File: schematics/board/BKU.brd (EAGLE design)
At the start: 94 x 94 mm, 48 parts

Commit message: Исправлена БСК1
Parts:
- BSK2, BSK4: device pinheadCS:1X10 -> pinheadCS:1X11
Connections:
- net 3V3: now also BSK2.8, BSK4.8
- net GND: now also BSK2.9, BSK4.9; no longer BSK2.8, BSK4.8
- net SCL-INA: now also BSK2.10, BSK4.10; no longer BSK2.9, BSK4.9
- net SDA-INA: now also BSK2.11, BSK4.11; no longer BSK2.10, BSK4.10
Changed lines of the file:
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@@
 </autorouter>
 <elements>
-<element name="BSK2" library="pinheadCS" package="1X10" value="" x="39" y="9.9" smashed="yes">
+<element name="BSK2" library="pinheadCS" package="1X11" value="" x="39" y="9.9" smashed="yes">
 <attribute name="NAME" x="28.7638" y="6.7288" size="1.27" layer="25" ratio="10"/>
 <attribute name="VALUE" x="28.84" y="6.725" size="1.27" layer="27"/>
@@
 <attribute name="VALUE" x="87.275" y="31.76" size="1.27" layer="27" rot="R90"/>
 </element>
-<element name="BSK4" library="pinheadCS" package="1X10" value="" x="47" y="84.1" smashed="yes" rot="R180">
+<element name="BSK4" library="pinheadCS" package="1X11" value="" x="47" y="84.1" smashed="yes" rot="R180">
 <attribute name="NAME" x="64.8562" y="87.2712" size="1.27" layer="25" ratio="10" rot="R180"/>
 <attribute name="VALUE" x="64.78" y="87.275" size="1.27" layer="27" rot="R180"/>
@@
 <contactref element="BSK1" pad="9"/>
 <contactref element="BSK1" pad="11"/>
-<contactref element="BSK4" pad="8"/>
 <contactref element="BSK3" pad="9"/>
-<contactref element="BSK2" pad="8"/>
+<contactref element="BSK2" pad="9"/>
+<contactref element="BSK4" pad="9"/>
 <wire x1="82.8114" y1="76.55" x2="80.8" y2="79.1" width="0" layer="19" extent="1-1"/>
 <wire x1="85" y1="69.8" x2="84.47" y2="71.76" width="0" layer="19" extent="1-1"/>
@@
 <wire x1="32.01939375" y1="6.288" x2="30.11" y2="1.2162" width="0" layer="19" extent="1-16"/>
 <wire x1="75.7222375" y1="10.7777625" x2="70.95" y2="8.15" width="0" layer="19" extent="1-1"/>
-<wire x1="45.35" y1="9.9" x2="50.2" y2="3.3" width="0" layer="19" extent="16-16"/>
+<wire x1="46.62" y1="9.9" x2="50.2" y2="3.3" width="0" layer="19" extent="16-16"/>
 <wire x1="69.98" y1="41.3" x2="70.45" y2="33.74" width="0" layer="19" extent="1-1"/>
 <wire x1="72.52" y1="41.3" x2="69.98" y2="41.3" width="0" layer="19" extent="1-1"/>
@@
 <wire x1="56.1" y1="23.91" x2="60.48" y2="24.27" width="0" layer="19" extent="1-1"/>
 <wire x1="61.1" y1="16.77" x2="63.23" y2="23.91" width="0" layer="19" extent="1-1"/>
-<wire x1="43.55" y1="17.2" x2="45.35" y2="9.9" width="0" layer="19" extent="1-1"/>
+<wire x1="43.55" y1="17.2" x2="46.62" y2="9.9" width="0" layer="19" extent="1-1"/>
 <wire x1="39.65" y1="20.6" x2="43.55" y2="17.2" width="0" layer="19" extent="1-1"/>
 <wire x1="48.65" y1="41.25" x2="56.02" y2="36.73" width="0" layer="19" extent="1-1"/>
@@
 <wire x1="28.66" y1="36.86" x2="30.46" y2="36.97" width="0" layer="19" extent="1-1"/>
 <wire x1="29.26" y1="16" x2="30.90739375" y2="7.4" width="0" layer="19" extent="1-1"/>
-<wire x1="40.65" y1="84.1" x2="43.19" y2="93" width="0" layer="19" extent="16-16"/>
+<wire x1="39.38" y1="84.1" x2="43.19" y2="93" width="0" layer="19" extent="16-16"/>
 <wire x1="21.76" y1="25.51" x2="28.79" y2="33.47" width="0" layer="19" extent="1-1"/>
 <wire x1="11.75" y1="30.215" x2="21.76" y2="25.51" width="0" layer="19" extent="1-1"/>
@@
 <wire x1="7.1" y1="30.8" x2="9.55" y2="33.3136" width="0" layer="19" extent="1-16"/>
 <wire x1="84.1" y1="48.27" x2="72.52" y2="41.3" width="0" layer="19" extent="1-1"/>
-<wire x1="53.5" y1="77.09" x2="66.1738" y2="87.657775" width="0" layer="19" extent="1-16"/>
+<wire x1="53.5" y1="77.09" x2="39.38" y2="84.1" width="0" layer="19" extent="1-1"/>
 <wire x1="53.5" y1="61.85" x2="53.5" y2="77.09" width="0" layer="19" extent="1-1"/>
 <wire x1="8.75" y1="13.88" x2="11.75" y2="30.215" width="0" layer="19" extent="1-1"/>
@@
 <wire x1="68.6014" y1="27.5514" x2="68.125" y2="30.425" width="0" layer="19" extent="1-16"/>
 <wire x1="70.45" y1="26.12" x2="68.6014" y2="26.5514" width="0" layer="19" extent="1-16"/>
-<wire x1="42.81" y1="9.9" x2="51.875" y2="11.25" width="0" layer="19" extent="16-16"/>
-<wire x1="28.5" y1="10.875" x2="42.81" y2="9.9" width="0" layer="19" extent="16-16"/>
+<wire x1="41.54" y1="9.9" x2="51.875" y2="11.25" width="0" layer="19" extent="16-16"/>
+<wire x1="28.5" y1="10.875" x2="41.54" y2="9.9" width="0" layer="19" extent="16-16"/>
 <wire x1="53.7282" y1="82.75163125" x2="77.60483125" y2="84.875" width="0" layer="19" extent="16-16"/>
-<wire x1="43.19" y1="84.1" x2="51.25" y2="79.39516875" width="0" layer="19" extent="16-16"/>
+<wire x1="44.46" y1="84.1" x2="51.25" y2="79.39516875" width="0" layer="19" extent="16-16"/>
 <wire x1="9.9" y1="61.89" x2="7.5" y2="25.5" width="0" layer="19" extent="1-1"/>
 </signal>
@@
 <wire x1="80.8875" y1="65.2375" x2="85" y2="64.6" width="0" layer="19" extent="1-16"/>
 <wire x1="84.1" y1="38.11" x2="85.125" y2="62.625" width="0" layer="19" extent="1-1"/>
-<wire x1="48.27" y1="84.1" x2="77.043625" y2="83.625" width="0" layer="19" extent="16-16"/>
-<wire x1="28.49" y1="84.6" x2="48.27" y2="84.1" width="0" layer="19" extent="16-16"/>
+<wire x1="49.54" y1="84.1" x2="77.043625" y2="83.625" width="0" layer="19" extent="16-16"/>
+<wire x1="28.49" y1="84.6" x2="49.54" y2="84.1" width="0" layer="19" extent="16-16"/>
 <wire x1="9.9" y1="66.97" x2="13" y2="66.625" width="0" layer="19" extent="16-16"/>
 <wire x1="5.5" y1="56.125" x2="13" y2="63.75" width="0" layer="19" extent="1-1"/>
 <wire x1="12" y1="37.125" x2="7.375" y2="43.25" width="0" layer="19" extent="16-16"/>
-<wire x1="37.73" y1="9.9" x2="27.125" y2="10.375" width="0" layer="19" extent="16-16"/>
+<wire x1="36.46" y1="9.9" x2="27.125" y2="10.375" width="0" layer="19" extent="16-16"/>
 </signal>
 <signal name="N$3">
@@
 <contactref element="BSK2" pad="6"/>
 <contactref element="BSK3" pad="6"/>
-<wire x1="58.43" y1="87.43" x2="45.73" y2="84.1" width="0" layer="19" extent="16-16"/>
+<wire x1="58.43" y1="87.43" x2="47" y2="84.1" width="0" layer="19" extent="16-16"/>
 <wire x1="7.1" y1="31.6" x2="8.5" y2="31.47" width="0" layer="19" extent="1-16"/>
 <wire x1="7.1" y1="36.4" x2="7.1" y2="31.6" width="0" layer="19" extent="1-1"/>
-<wire x1="40.27" y1="9.9" x2="47.89" y2="9.601315625" width="0" layer="19" extent="16-16"/>
+<wire x1="39" y1="9.9" x2="47.89" y2="9.601315625" width="0" layer="19" extent="16-16"/>
 <wire x1="84.1" y1="40.65" x2="92.1206" y2="39.1632" width="0" layer="19" extent="16-16"/>
 <wire x1="9.9" y1="64.43" x2="8.5" y2="42.71" width="0" layer="19" extent="16-16"/>
@@
 <contactref element="BSK1" pad="8"/>
 <contactref element="BSK3" pad="8"/>
-<wire x1="9.9" y1="59.35" x2="84.1" y2="45.73" width="0" layer="19" extent="1-1"/>
+<contactref element="BSK2" pad="8"/>
+<contactref element="BSK4" pad="8"/>
+<wire x1="44.08" y1="9.9" x2="84.1" y2="45.73" width="0" layer="19" extent="1-1"/>
+<wire x1="41.92" y1="84.1" x2="84.1" y2="45.73" width="0" layer="19" extent="1-1"/>
+<wire x1="9.9" y1="59.35" x2="41.92" y2="84.1" width="0" layer="19" extent="1-1"/>
 </signal>
 <signal name="PL6-KVCC">
@@
 </signal>
 <signal name="SCL-INA">
-<contactref element="BSK2" pad="9"/>
 <contactref element="BSK3" pad="15"/>
-<contactref element="BSK4" pad="9"/>
-<wire x1="38.11" y1="84.1" x2="84.1" y2="63.51" width="0" layer="19" extent="1-1"/>
-<wire x1="47.89" y1="9.9" x2="84.1" y2="63.51" width="0" layer="19" extent="1-1"/>
+<contactref element="BSK2" pad="10"/>
+<contactref element="BSK4" pad="10"/>
+<wire x1="36.84" y1="84.1" x2="84.1" y2="63.51" width="0" layer="19" extent="1-1"/>
+<wire x1="49.16" y1="9.9" x2="84.1" y2="63.51" width="0" layer="19" extent="1-1"/>
 </signal>
 <signal name="SDA-INA">
-<contactref element="BSK2" pad="10"/>
 <contactref element="BSK3" pad="16"/>
-<contactref element="BSK4" pad="10"/>
-<wire x1="35.57" y1="84.1" x2="84.1" y2="66.05" width="0" layer="19" extent="1-1"/>
-<wire x1="50.43" y1="9.9" x2="84.1" y2="66.05" width="0" layer="19" extent="1-1"/>
+<contactref element="BSK2" pad="11"/>
+<contactref element="BSK4" pad="11"/>
+<wire x1="34.3" y1="84.1" x2="84.1" y2="66.05" width="0" layer="19" extent="1-1"/>
+<wire x1="51.7" y1="9.9" x2="84.1" y2="66.05" width="0" layer="19" extent="1-1"/>
 </signal>
 </signals>

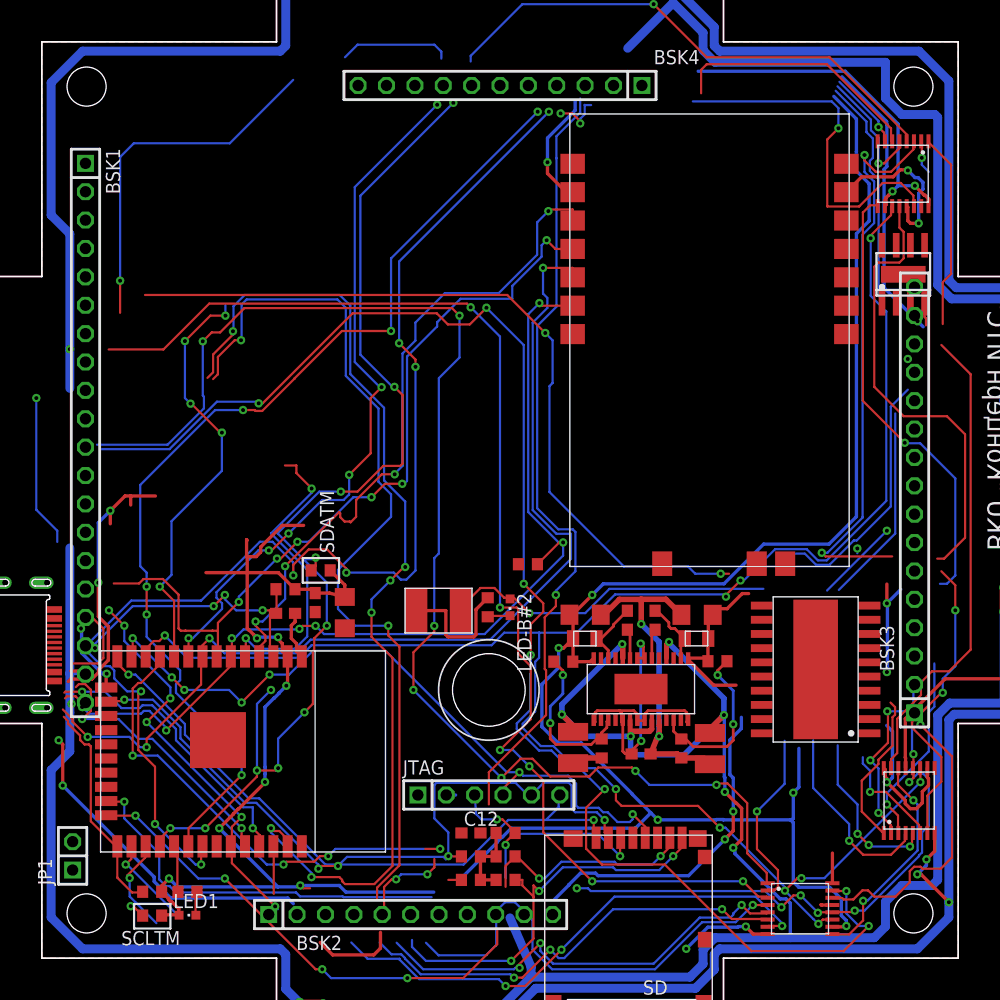
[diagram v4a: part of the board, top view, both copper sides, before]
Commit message: Обновлен список плат, работа над платой ПН
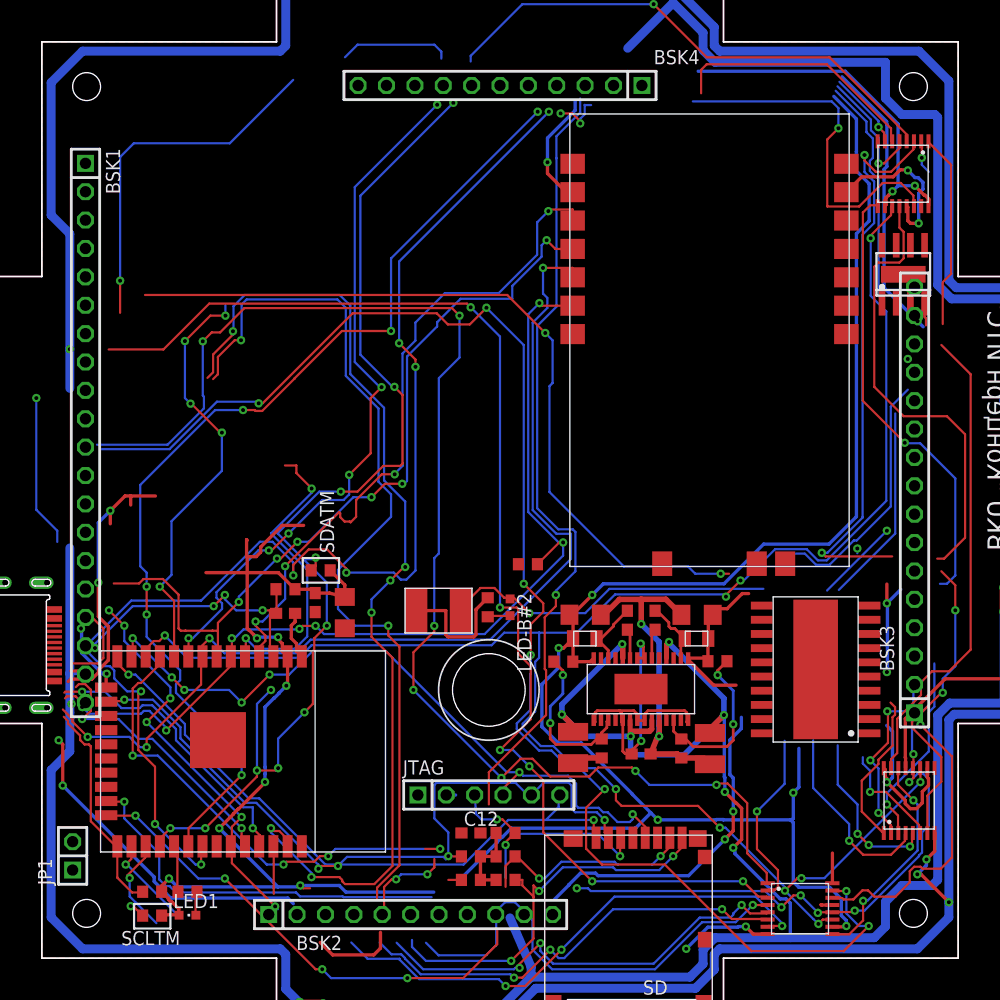
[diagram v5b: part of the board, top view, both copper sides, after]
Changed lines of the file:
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@@
 <layer number="43" name="vRestrict" color="2" fill="10" visible="no" active="yes"/>
 <layer number="44" name="Drills" color="7" fill="1" visible="no" active="yes"/>
-<layer number="45" name="Holes" color="7" fill="1" visible="no" active="yes"/>
+<layer number="45" name="Holes" color="7" fill="1" visible="yes" active="yes"/>
 <layer number="46" name="Milling" color="3" fill="1" visible="no" active="yes"/>
 <layer number="47" name="Measures" color="7" fill="1" visible="no" active="yes"/>
@@
 <wire x1="6" y1="6" x2="27" y2="6" width="0.1524" layer="20"/>
 <wire x1="27" y1="6" x2="27" y2="0" width="0.1524" layer="20"/>
-<hole x="10" y="10" drill="3.5"/>
-<hole x="84" y="84" drill="3.5"/>
-<hole x="10" y="84" drill="3.5"/>
-<hole x="84" y="10" drill="3.5"/>
+<hole x="10" y="10" drill="2.5"/>
+<hole x="84" y="84" drill="2.5"/>
+<hole x="10" y="84" drill="2.5"/>
+<hole x="84" y="10" drill="2.5"/>
 <text x="92.4" y="64.95" size="1.778" layer="25" rot="MR270">BKU "Концерн ИТС"</text>
 <wire x1="0" y1="67" x2="0" y2="38.5" width="0.1524" layer="20"/>

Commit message: Схема БКУ
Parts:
- removed JP1: (no value), pinheadCS:1X02
- removed JTAG: (no value), pinheadCS:1X06
- removed LED-B#2: (no value), led:CHIPLED_0603
- removed R27: 2k, resistor:R0603
- removed R29: 10k, resistor:R0603
- removed RADIO: RADIO, CanCubeSat:RADIO
- removed U$6: USB-C, CanCubeSat:USB-C
- removed U$7: EM_HEAT, CanCubeSat:EM_HEAT
- removed U$8: L293DD, CanCubeSat:L293DD
- added LED-G, LED_B1: (no value), led:CHIPLED_0603
- added R1: 5k1, resistor:R0603
- added R14, R16, R4: 1M, resistor:R0603
- added R15: 0.05A, rcl:R1210
- added R17, R31, R32: 100R, resistor:R0603
- added R19, R33: 0.5A, rcl:R1210
- added R3, R7: 2k, resistor:R0603
- added U$1: E22-400M30S, CanCubeSat:E22-400M30S
- added U$2: 74HC595, CanCubeSat:74HC595
- added U$21: FFC-CONNECT68611, CanCubeSat:68611
- added U$23, U$3, U$4: SI2302CDS, CanCubeSat:SOT23-3
- added U$24: EM_HEAT, CanCubeSat:EM_HEAT
- BSK3: device pinheadCS:1X16 -> pinheadCS:1X14
- moved C15 73.4 mm to (86.6, -33.3)
- moved C16 73.4 mm to (87.8, -45.2)
- moved C17 73.4 mm to (75.5, -45.1)
- moved C5 73.4 mm to (80.4, -33.8)
- moved C6 73.4 mm to (76.6, -33.3)
- moved R12 73.4 mm to (88.5, -37.4)
- moved R13 73.4 mm to (74.7, -37.5)
- moved R9 73.4 mm to (85.2, -45.2)
- moved U$11 73.4 mm to (76.6, -35.4)
- moved U$12 73.4 mm to (86.6, -35.4)
- moved C1 73.4 mm to (82.9, -33.8)
- moved C14 73.4 mm to (81.6, -45.7)
- moved R8 73.4 mm to (78.1, -45.2)
- moved U$10 73.4 mm to (81.6, -39.9)
- moved BSK1 66.5 mm to (44.0, -4.10), turned to 0 degrees
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- renumbered LED1 to LED-B
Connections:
- removed net AUX: RADIO.P$5, U$13.4
- removed net B1_KEM+: U$18.2, U$8.2
- removed net B1_KEM-: U$18.3, U$8.9
- removed net B1_KHEAT: U$18.1, U$8.19
- removed net B2A_KEM+: U$19.2
- removed net B2A_KEM-: U$19.3
- removed net B2A_KHEAT: U$19.1
- removed net B2A_KVCC: U$19.15
- removed net B2_KEM+: U$19.6
- removed net B2_KEM-: U$19.7
- removed net B2_KHEAT: U$19.5
- removed net B2_KVCC: U$19.4
- removed net B3_KEM+: U$20.6
- removed net B3_KEM-: U$20.7
- removed net B3_KHEAT: U$20.5
- removed net B3_KVCC: U$20.4
- removed net B4_KEM+: U$18.6
- removed net B4_KEM-: U$18.7
- removed net B4_KHEAT: U$18.5
- removed net B4_KVCC: U$18.4
- removed net B5-CMD: BSK3.13
- removed net B5-KVCC: BSK3.11
- removed net B5-ROZE: BSK3.12
- removed net B5_KEM+: U$20.2
- removed net B5_KEM-: U$20.3
- removed net B5_KHEAT: U$20.1
- removed net B5_KVCC: U$20.15
- removed net DS: U$13.10, U$18.14
- removed net I2CINT: U$13.30
- removed net M1: R29.1, RADIO.P$2, U$13.6, U$6.NC/M1
- removed net N$51: LED-B#2.C, R27.1
- removed net PL_KVCC: U$13.9
- removed net RX-ES: U$13.36
- removed net SCL-INA: BSK2.10, BSK3.15, BSK4.10
- removed net SDA-INA: BSK2.11, BSK3.16, BSK4.11
- removed net SHCP: U$13.12, U$18.11, U$19.11, U$20.11
- removed net STCP: U$13.11, U$18.12, U$19.12, U$20.12
- removed net TX-ES: U$13.37
- removed net VDD: C12.2, C3.1, C33.1, C6.1, JTAG.2, LED-B.A, R10.1, R11.1, R13.2, R18.1, R21.1, R22.1, R23.1, R24.1, R5.2, R6.2, SD.VDD, U$10.28, U$11.2, U$13.2, U$18.10, U$18.16, U$19.10, U$19.16, U$20.10, U$20.16, U$6.NC/3V3
- new net 3: R3.2, U$23.3, U$24.2
- new net BKU-KHEAT: U$2.15
- new net BUSY: U$1.14, U$13.7
- new net CS-RA: U$1.19, U$13.33
- new net CS-SR: U$13.31, U$18.12, U$19.12, U$2.12, U$20.12
- new net DIO1: U$1.13, U$13.8
- new net GND-OUT: BSK1.11, BSK1.9, BSK2.9, BSK3.14, BSK3.9, BSK4.9, R33.2, U$21.P$11, U$21.P$5, U$21.P$7, U$21.P$9
- new net GND-RADIO: R19.2, U$4.3
- new net GND-SD: R15.1, U$3.3
- new net MISO: U$1.16, U$13.4
- new net MOSI: U$1.17, U$13.37, U$18.14
- new net N$1: U$2.14, U$20.9
- new net N$11: R14.1, R31.2, U$3.1
- new net N$2: LED_B1.C, R3.1
- new net N$36: R32.1, R4.1, U$23.1
- new net N$5: R15.2, SD.VSS
- new net N$6: R16.1, R17.2, U$4.1
- new net NRST: R1.1, U$1.15, U$13.9
- new net RADIO: R17.1, U$2.2
- new net RX-EN: U$1.6, U$13.11
- new net SCK: U$1.18, U$13.36, U$18.11, U$19.11, U$2.11, U$20.11
- new net SD: R31.1, U$2.1
- new net TX-EN: U$1.7, U$13.10
- net 1W: now also U$13.12; no longer U$13.33
- net 3V3: now also C12.2, C3.1, C33.1, C6.1, LED-B.A, LED-G.A, R1.2, R10.1, R11.1, R13.2, R18.1, R21.1, R22.1, R23.1, R24.1, R5.2, R6.2, SD.VDD, U$10.28, U$11.2, U$13.2, U$18.10, U$18.16, U$19.10, U$19.16, U$2.10, U$2.16, U$20.10, U$20.16, U$21.P$3
- net 5V: now also LED_B1.A, U$1.10, U$1.9, U$24.1; no longer RADIO.P$6, U$8.1, U$8.10, U$8.11, U$8.20
- net B1-CMD: now also U$18.3
- net B1-KHEAT: now also R32.2, U$18.15
- net B1-KVCC: now also U$18.1
- net B1-ROZE: now also U$18.2
- net B2-CMD: now also U$18.7
- net B2-KHEAT: now also U$18.4
- net B2-KVCC: now also U$18.5
- net B2-ROZE: now also U$18.6
- net B3-CMD: now also U$19.3
- net B3-KHEAT: now also U$19.15
- net B3-KVCC: now also U$19.1
- net B3-ROZE: now also U$19.2
- net B4-CMD: now also U$19.7
- net B4-KHEAT: now also U$19.4
- net B4-KVCC: now also U$19.5
- net B4-ROZE: now also U$19.6
- net B5-KHEAT: now also U$20.15
- net BUS+: now also U$21.P$1, U$21.P$2; no longer U$6.3V3/BUS0, U$6.3V3/BUS1
- net DAT0: now also U$21.P$14; no longer JP1.2
- net EN: now also U$21.P$4; no longer U$6.NRST/EN
- net GND: now also R14.2, R16.2, R19.1, R33.1, R4.2, R7.1, U$1.1, U$1.11, U$1.12, U$1.2, U$1.20, U$1.22, U$1.3, U$1.4, U$1.5, U$2.13, U$2.8, U$23.2, U$3.2, U$4.2; no longer BSK1.11, BSK1.9, BSK2.9, BSK3.9, BSK4.9, JP1.1, JTAG.1, R27.2, R29.2, RADIO.P$1, RADIO.P$15, RADIO.P$16, RADIO.P$17, RADIO.P$7, RADIO.P$9, SD.VSS, U$6.GND0, U$6.GND1, U$7.2, U$8.14, U$8.15, U$8.16, U$8.17, U$8.4, U$8.5, U$8.6, U$8.7, U$8.HEAT
- net IO0-E: now also U$21.P$13; no longer U$6.NC/GPIO
- net MTCK: no longer JTAG.5
- net MTDI: no longer JTAG.6
- net MTDO: no longer JTAG.3
- net MTMS: no longer JTAG.4
- net N$3: now also LED-G.C, R7.2; no longer LED-B#2.A, U$7.1, U$8.18
- net PL1-KVCC: now also U$20.2
- net PL2-KVCC: now also U$20.3
- net PL3-KVCC: now also U$20.4
- net PL4-KVCC: now also U$20.5
- net PL5-KVCC: now also U$20.6
- net PL6-KVCC: now also U$20.7
- net RX-E: now also U$21.P$6; no longer U$6.SWD/RXD
- net RX-R: now also U$21.P$10; no longer RADIO.P$4, U$13.7, U$6.RX0
- net SCL-TM: now also BSK2.10, BSK3.12, BSK4.10
- net SDA-TM: now also BSK2.11, BSK3.13, BSK4.11
- net SINS-KVCC: now also BSK3.11, U$20.1; no longer BSK3.14
- net TIME: now also U$13.30; no longer U$13.31
- net TX-E: now also U$21.P$8; no longer U$6.SWC/TXD
- net TX-R: now also U$21.P$12; no longer RADIO.P$3, U$13.8, U$6.TX0
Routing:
- net GND: track 378.1 -> 0.00 mm, vias 13 -> 0
- net VDD: track 325.5 -> 0.00 mm, vias 17 -> 0
- net BUS+: track 321.0 -> 0.00 mm, vias 13 -> 0
- net SHCP: track 165.6 -> 0.00 mm, vias 10 -> 0
- net STCP: track 136.0 -> 0.00 mm, vias 11 -> 0
- net B2A_KVCC: track 133.4 -> 0.00 mm, vias 7 -> 0
- net 5V: track 122.3 -> 0.00 mm, vias 8 -> 0
- net B2A_KHEAT: track 120.9 -> 0.00 mm, vias 7 -> 0
- net TIME: track 112.9 -> 0.00 mm, vias 8 -> 0
- net B2A_KEM-: track 110.3 -> 0.00 mm, vias 6 -> 0
- net 1W: track 103.9 -> 0.00 mm, vias 8 -> 0
- net SDA-TM: track 100.3 -> 0.00 mm, vias 11 -> 0
- net I2CINT: track 91.7 -> 0.00 mm, vias 6 -> 0
- net TX-R: track 90.0 -> 0.00 mm, vias 4 -> 0
- net TX-ES: track 89.7 -> 0.00 mm, vias 6 -> 0
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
